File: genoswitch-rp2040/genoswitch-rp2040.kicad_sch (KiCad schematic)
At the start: 35 parts, among them J1 USB_B_Micro, J2 Conn_01x03_Socket-PicoDebug, J3 HW-SPI0, J4 HW-SPI1, J5 PIO-SPI0, J6 PIO-SPI1, SW1 PTS815_SJM_250_SMTR_LFS, U1 NCP1117-3.3_SOT223, U2 W25Q128JVS, U3 RP2040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

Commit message: Change 0603 components to 0402 sizes
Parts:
- C1, C10, C101, C11, C12, C13, C14, C15, C16, C4, C6, C7, C8, C9: footprint Capacitor_SMD:C_0201_0603Metric -> Capacitor_SMD:C_01005_0402Metric
- R1, R2, R3, R4, R5: footprint Resistor_SMD:R_0201_0603Metric -> Resistor_SMD:R_01005_0402Metric
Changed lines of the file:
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@@
       (effects (font (size 1.27 1.27)) (justify left))
     )
-    (property "Footprint" "Capacitor_SMD:C_0201_0603Metric" (at 70.8152 31.75 0)
+    (property "Footprint" "Capacitor_SMD:C_01005_0402Metric" (at 70.8152 31.75 0)
       (effects (font (size 1.27 1.27)) hide)
     )
@@
       (effects (font (size 1.27 1.27)) (justify left))
     )
-    (property "Footprint" "Resistor_SMD:R_0201_0603Metric" (at 168.402 25.4 90)
+    (property "Footprint" "Resistor_SMD:R_01005_0402Metric" (at 168.402 25.4 90)
       (effects (font (size 1.27 1.27)) hide)
     )
@@
       (effects (font (size 1.27 1.27)) (justify left))
     )
-    (property "Footprint" "Resistor_SMD:R_0201_0603Metric" (at 168.402 35.56 90)
+    (property "Footprint" "Resistor_SMD:R_01005_0402Metric" (at 168.402 35.56 90)
       (effects (font (size 1.27 1.27)) hide)
     )
@@
       (effects (font (size 1.27 1.27)))
     )
-    (property "Footprint" "Resistor_SMD:R_0201_0603Metric" (at 349.25 178.308 90)
+    (property "Footprint" "Resistor_SMD:R_01005_0402Metric" (at 349.25 178.308 90)
       (effects (font (size 1.27 1.27)) hide)
     )
@@
       (effects (font (size 1.27 1.27)) (justify left))
     )
-    (property "Footprint" "Capacitor_SMD:C_0201_0603Metric" (at 108.9152 31.75 0)
+    (property "Footprint" "Capacitor_SMD:C_01005_0402Metric" (at 108.9152 31.75 0)
       (effects (font (size 1.27 1.27)) hide)
     )
@@
       (effects (font (size 1.27 1.27)) (justify left))
     )
-    (property "Footprint" "Capacitor_SMD:C_0201_0603Metric" (at 39.0652 31.75 0)
+    (property "Footprint" "Capacitor_SMD:C_01005_0402Metric" (at 39.0652 31.75 0)
       (effects (font (size 1.27 1.27)) hide)
     )
@@
       (effects (font (size 1.27 1.27)))
     )
-    (property "Footprint" "Resistor_SMD:R_0201_0603Metric" (at 351.79 38.862 90)
+    (property "Footprint" "Resistor_SMD:R_01005_0402Metric" (at 351.79 38.862 90)
       (effects (font (size 1.27 1.27)) hide)
     )
@@
       (effects (font (size 1.27 1.27)) (justify right))
     )
-    (property "Footprint" "Capacitor_SMD:C_0201_0603Metric" (at 190.8048 179.07 0)
+    (property "Footprint" "Capacitor_SMD:C_01005_0402Metric" (at 190.8048 179.07 0)
       (effects (font (size 1.27 1.27)) hide)
     )
@@
       (effects (font (size 1.27 1.27)) (justify left))
     )
-    (property "Footprint" "Capacitor_SMD:C_0201_0603Metric" (at 51.7652 44.45 0)
+    (property "Footprint" "Capacitor_SMD:C_01005_0402Metric" (at 51.7652 44.45 0)
       (effects (font (size 1.27 1.27)) hide)
     )
@@
       (effects (font (size 1.27 1.27)) (justify left))
     )
-    (property "Footprint" "Capacitor_SMD:C_0201_0603Metric" (at 171.1452 49.53 0)
+    (property "Footprint" "Capacitor_SMD:C_01005_0402Metric" (at 171.1452 49.53 0)
       (effects (font (size 1.27 1.27)) hide)
     )
@@
       (effects (font (size 1.27 1.27)) (justify left))
     )
-    (property "Footprint" "Capacitor_SMD:C_0201_0603Metric" (at 53.0352 31.75 0)
+    (property "Footprint" "Capacitor_SMD:C_01005_0402Metric" (at 53.0352 31.75 0)
       (effects (font (size 1.27 1.27)) hide)
     )
@@
       (effects (font (size 1.27 1.27)) (justify left))
     )
-    (property "Footprint" "Capacitor_SMD:C_0201_0603Metric" (at 398.4752 231.14 0)
+    (property "Footprint" "Capacitor_SMD:C_01005_0402Metric" (at 398.4752 231.14 0)
       (effects (font (size 1.27 1.27)) hide)
     )
@@
       (effects (font (size 1.27 1.27)) (justify left))
     )
-    (property "Footprint" "Capacitor_SMD:C_0201_0603Metric" (at 107.6452 53.34 0)
+    (property "Footprint" "Capacitor_SMD:C_01005_0402Metric" (at 107.6452 53.34 0)
       (effects (font (size 1.27 1.27)) hide)
     )
@@
       (effects (font (size 1.27 1.27)) (justify left))
     )
-    (property "Footprint" "Capacitor_SMD:C_0201_0603Metric" (at 121.6152 31.75 0)
+    (property "Footprint" "Capacitor_SMD:C_01005_0402Metric" (at 121.6152 31.75 0)
       (effects (font (size 1.27 1.27)) hide)
     )
@@
       (effects (font (size 1.27 1.27)) (justify left))
     )
-    (property "Footprint" "Capacitor_SMD:C_0201_0603Metric" (at 96.2152 31.75 0)
+    (property "Footprint" "Capacitor_SMD:C_01005_0402Metric" (at 96.2152 31.75 0)
       (effects (font (size 1.27 1.27)) hide)
     )
@@
       (effects (font (size 1.27 1.27)) (justify left))
     )
-    (property "Footprint" "Capacitor_SMD:C_0201_0603Metric" (at 83.5152 31.75 0)
+    (property "Footprint" "Capacitor_SMD:C_01005_0402Metric" (at 83.5152 31.75 0)
       (effects (font (size 1.27 1.27)) hide)
     )
@@
       (effects (font (size 1.27 1.27)) (justify left))
     )
-    (property "Footprint" "Capacitor_SMD:C_0201_0603Metric" (at 329.8952 231.14 0)
+    (property "Footprint" "Capacitor_SMD:C_01005_0402Metric" (at 329.8952 231.14 0)
       (effects (font (size 1.27 1.27)) hide)
     )
@@
       (effects (font (size 1.27 1.27)) (justify right))
     )
-    (property "Footprint" "Resistor_SMD:R_0201_0603Metric" (at 367.538 35.56 90)
+    (property "Footprint" "Resistor_SMD:R_01005_0402Metric" (at 367.538 35.56 90)
       (effects (font (size 1.27 1.27)) hide)
     )
@@
       (effects (font (size 1.27 1.27)) (justify left))
     )
-    (property "Footprint" "Capacitor_SMD:C_0201_0603Metric" (at 134.3152 31.75 0)
-      (effects (font (size 1.27 1.27)) hide)
-    )
+    (property "Footprint" "Capacitor_SMD:C_01005_0402Metric" (at 134.3152 31.75 0)
+      (effects (font (size 1.27 1.27)) hide)
+    )

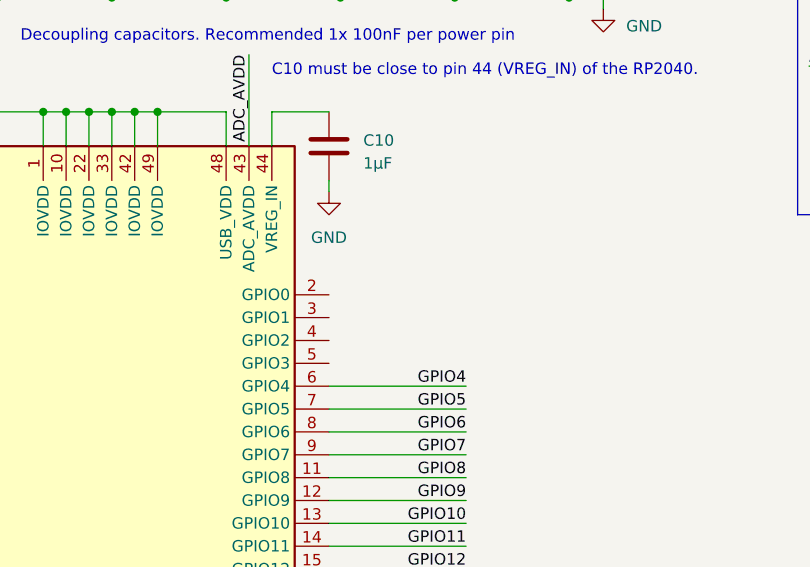
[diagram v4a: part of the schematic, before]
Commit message: Add serial header to RP2040
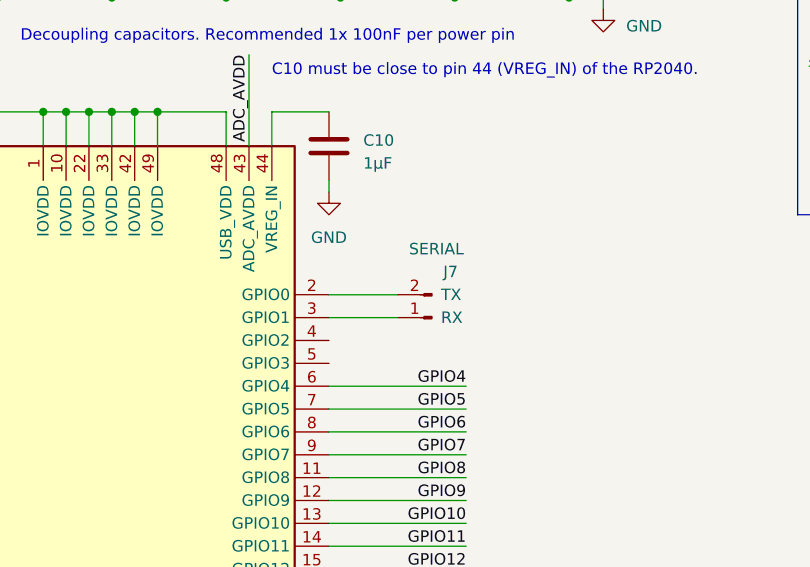
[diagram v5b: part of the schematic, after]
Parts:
- added J7: SERIAL, Connector_PinHeader_2.54mm:PinHeader_1x02_P2.54mm_Vertical, symbol Genoswitch_Custom:Serial_THT
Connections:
- net at U3.2 (GPIO0): now also J7.2 (TX)
- net at U3.3 (GPIO1): now also J7.1 (RX)
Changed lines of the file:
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@@
+    (stroke (width 0) (type default))
+  )
+  (wire (pts (xy 106.68 66.04) (xy 114.3 66.04))
     (stroke (width 0) (type default))
   )
@@
   )
   (wire (pts (xy 388.62 40.64) (xy 388.62 52.07))
+    (stroke (width 0) (type default))
+  )
+  (wire (pts (xy 106.68 68.58) (xy 114.3 68.58))
     (stroke (width 0) (type default))
   )
@@
         )
       )
+    )
+  )
+  (symbol (lib_id "Genoswitch_Custom:Serial_THT") (at 118.11 68.58 180) (unit 1)
+    (in_bom yes) (on_board yes) (dnp no)
+    (property "Reference" "J7" (at 119.38 63.5 0)
+      (effects (font (size 1.27 1.27)) (justify right))
+    )
+    (property "Value" "SERIAL" (at 115.57 60.96 0)
+      (effects (font (size 1.27 1.27)) (justify right))
+    )
+    (property "Footprint" "Connector_PinHeader_2.54mm:PinHeader_1x02_P2.54mm_Vertical" (at 118.11 68.58 0)
+      (effects (font (size 1.27 1.27)) hide)
+    )
+    (property "Datasheet" "~" (at 118.11 68.58 0)
+      (effects (font (size 1.27 1.27)) hide)
+    )
+    (pin "1")
+    (pin "2")
+    (instances
+      (project "genoswitch-rp2040"
+        (path "/2e7ee4d9-1204-4a0f-bb2c-fb0f0d4af2cf"
+          (reference "J7") (unit 1)
+        )
+      )

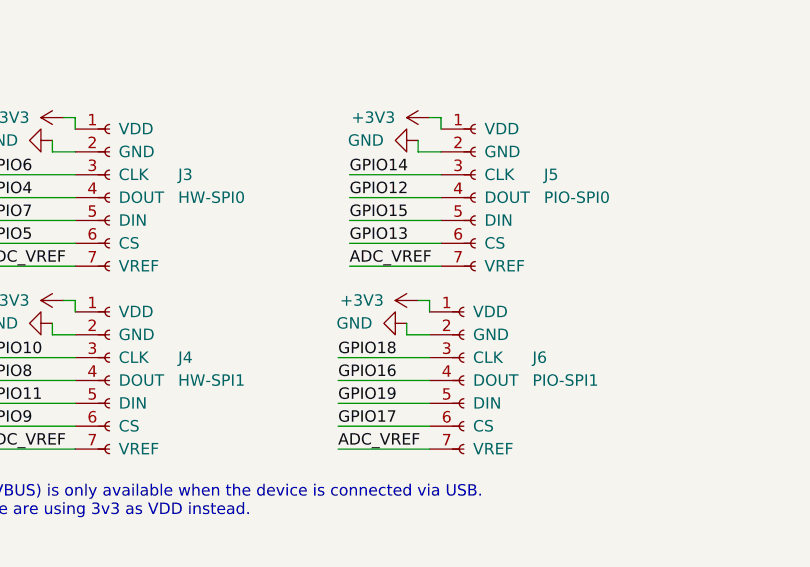
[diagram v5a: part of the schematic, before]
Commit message: Swap to horizonal JST PH connector
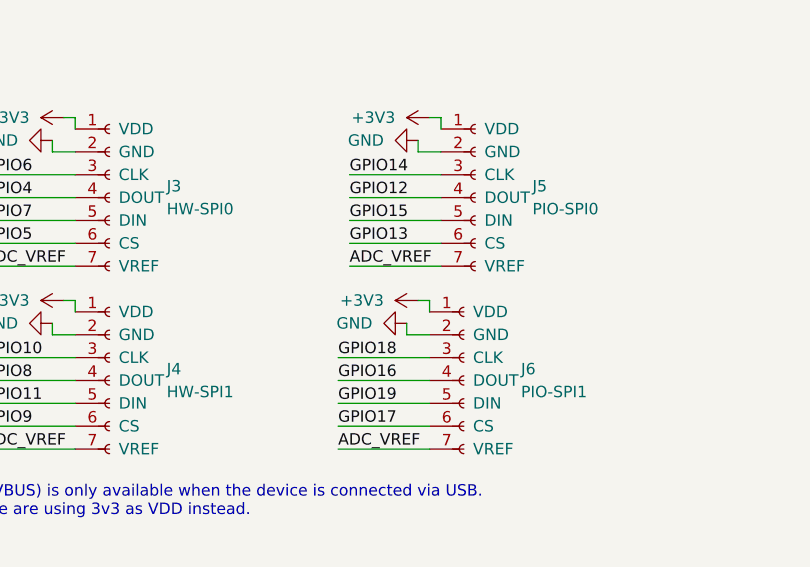
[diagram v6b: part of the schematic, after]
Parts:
- J3, J4, J5, J6: footprint Connector_JST:JST_PH_B7B-PH-K_1x07_P2.00mm_Vertical -> Connector_JST:JST_PH_S7B-PH-K_1x07_P2.00mm_Horizontal

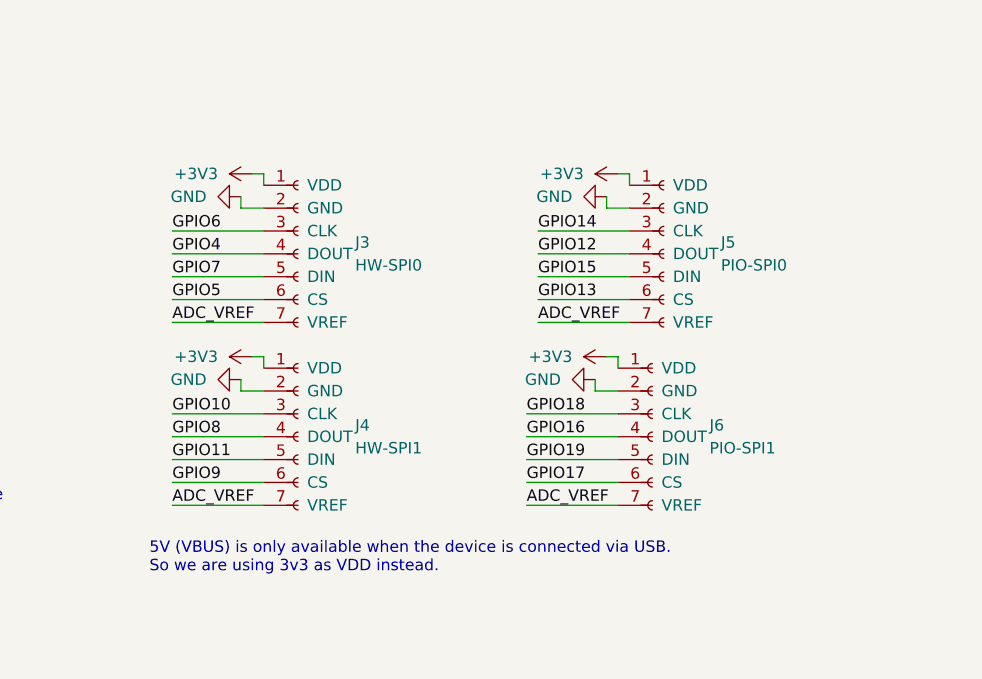
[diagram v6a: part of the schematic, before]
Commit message: (ADC_CONN): Make GND pin 1
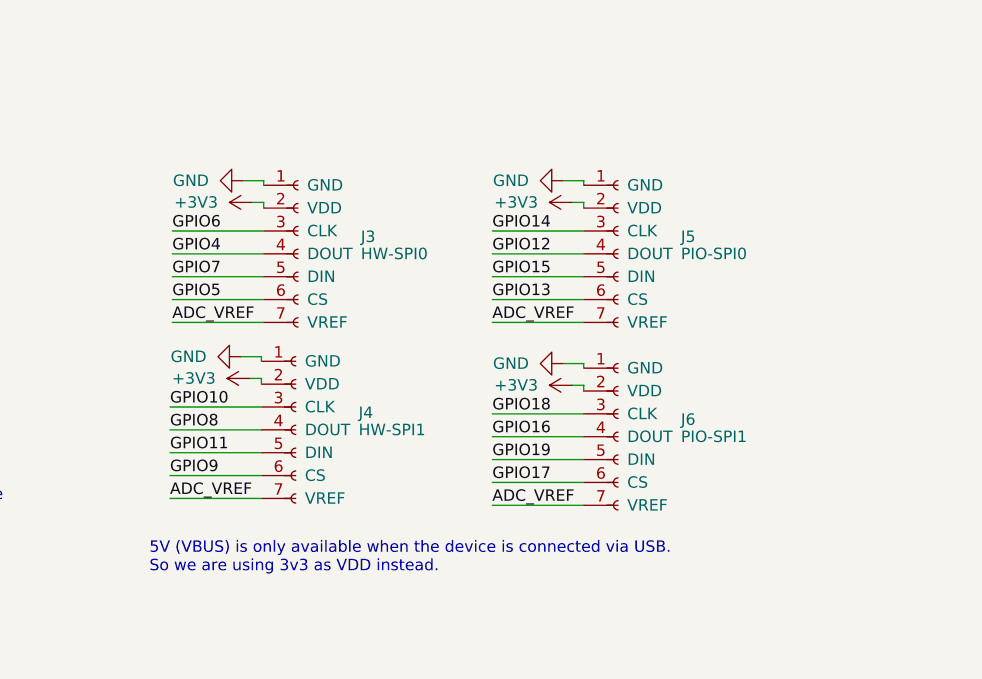
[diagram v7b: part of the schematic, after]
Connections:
- net +3V3: now also J3.2 (VDD), J4.2 (VDD), J5.2 (VDD), J6.2 (VDD); no longer J3.1 (VDD), J4.1 (VDD), J5.1 (VDD), J6.1 (VDD)
- net GND: now also J3.1 (GND), J4.1 (GND), J5.1 (GND), J6.1 (GND); no longer J3.2 (GND), J4.2 (GND), J5.2 (GND), J6.2 (GND)

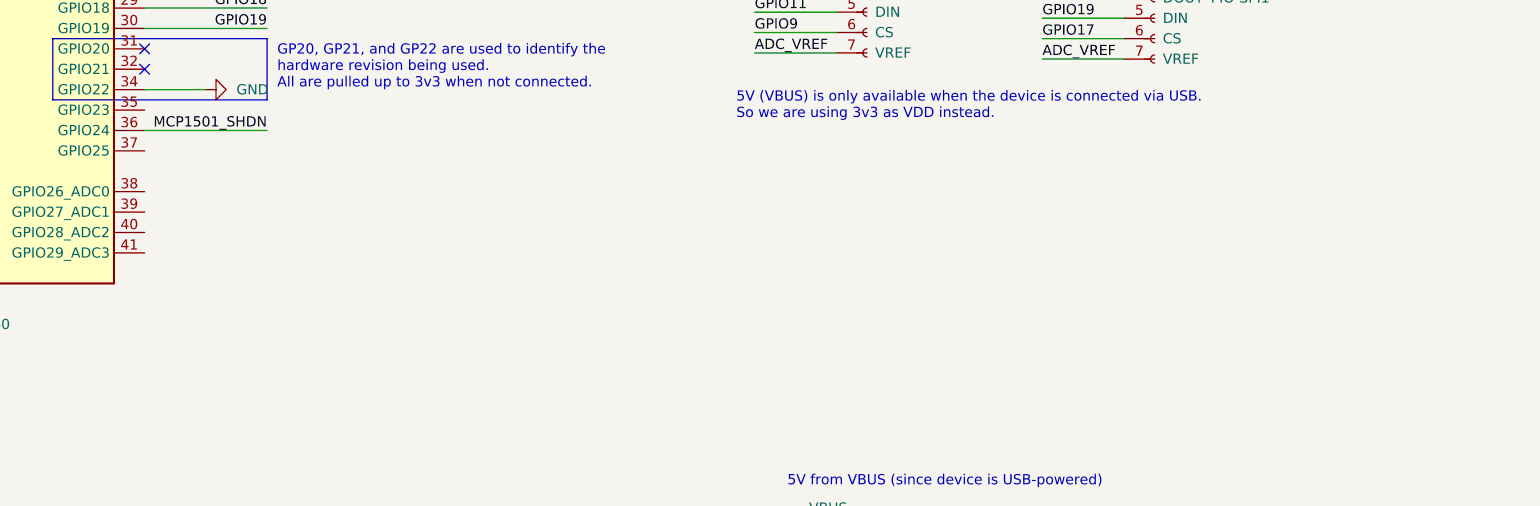
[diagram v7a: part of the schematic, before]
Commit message: Add ADC Channel sockets x4, place on board 5mil apart
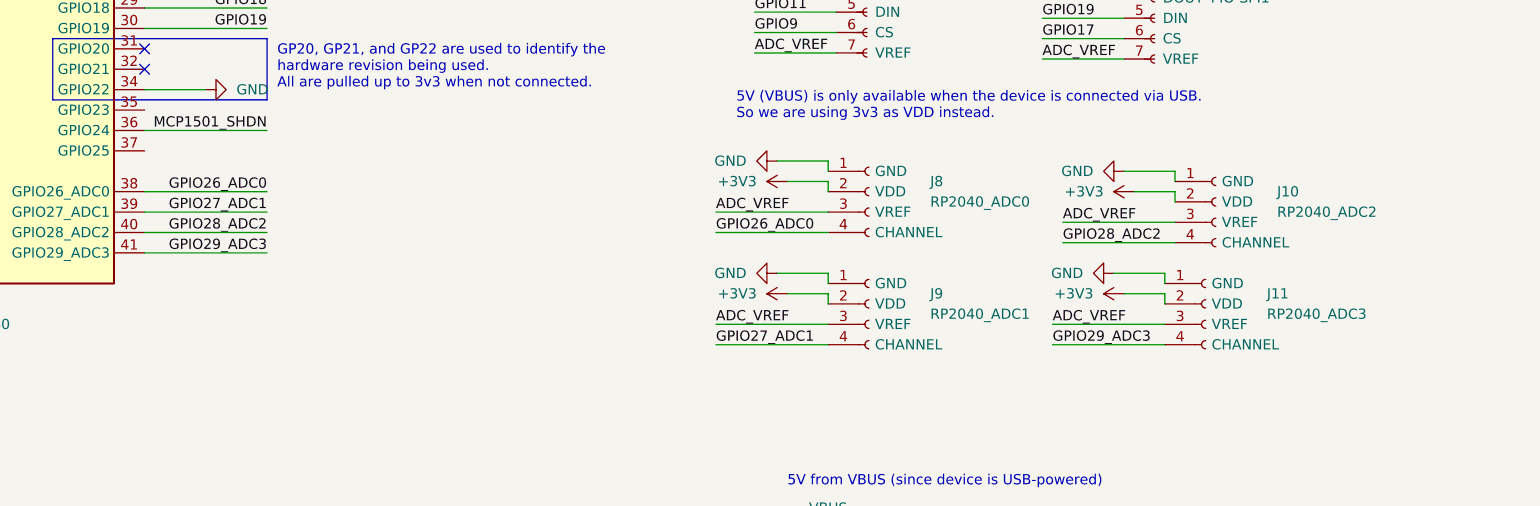
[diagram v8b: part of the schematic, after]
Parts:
- added J10: RP2040_ADC2, Connector_JST:JST_PH_S4B-PH-K_1x04_P2.00mm_Horizontal, symbol Genoswitch_Custom:GS_ADC_Channel_Socket
- added J11: RP2040_ADC3, Connector_JST:JST_PH_S4B-PH-K_1x04_P2.00mm_Horizontal, symbol Genoswitch_Custom:GS_ADC_Channel_Socket
- added J8: RP2040_ADC0, Connector_JST:JST_PH_S4B-PH-K_1x04_P2.00mm_Horizontal, symbol Genoswitch_Custom:GS_ADC_Channel_Socket
- added J9: RP2040_ADC1, Connector_JST:JST_PH_S4B-PH-K_1x04_P2.00mm_Horizontal, symbol Genoswitch_Custom:GS_ADC_Channel_Socket
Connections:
- net +3V3: now also J10.2 (VDD), J11.2 (VDD), J8.2 (VDD), J9.2 (VDD)
- net ADC_VREF: now also J10.3 (VREF), J11.3 (VREF), J8.3 (VREF), J9.3 (VREF)
- net GND: now also J10.1 (GND), J11.1 (GND), J8.1 (GND), J9.1 (GND)
- net GPIO26_ADC0: now reaches U3.38 (GPIO26_ADC0)
- net GPIO26_ADC0: now also J8.4 (CHANNEL)
- net GPIO27_ADC1: now reaches U3.39 (GPIO27_ADC1)
- net GPIO27_ADC1: now also J9.4 (CHANNEL)
- net GPIO28_ADC2: now reaches U3.40 (GPIO28_ADC2)
- net GPIO28_ADC2: now also J10.4 (CHANNEL)
- net GPIO29_ADC3: now reaches U3.41 (GPIO29_ADC3)
- net GPIO29_ADC3: now also J11.4 (CHANNEL)
